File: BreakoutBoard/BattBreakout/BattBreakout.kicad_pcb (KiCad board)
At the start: 2 copper layers, 67.3 x 52.1 mm, 22 parts, among them Q4 IPB180N10S4-02, Q9 IPB180N10S4-02, U2 LM5050MK-1_NOPB, U3 LM5050MK-1_NOPB

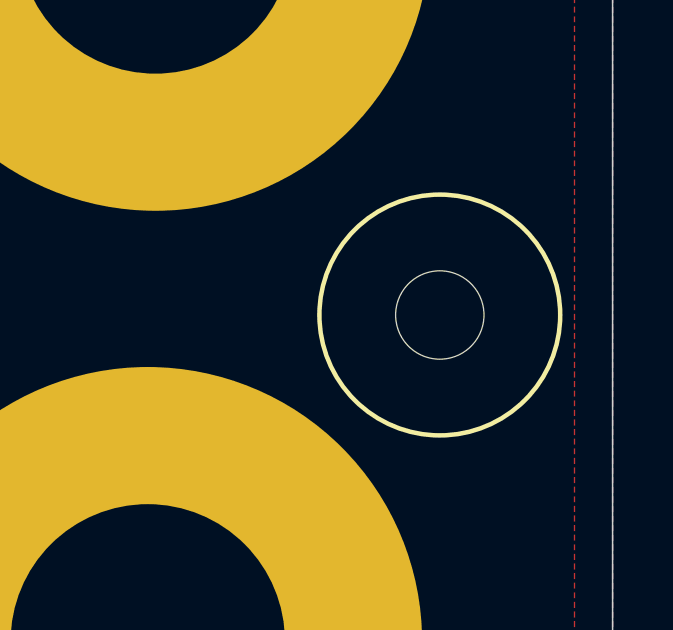
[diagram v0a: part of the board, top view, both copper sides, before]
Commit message: Added Ore to Breakout Board
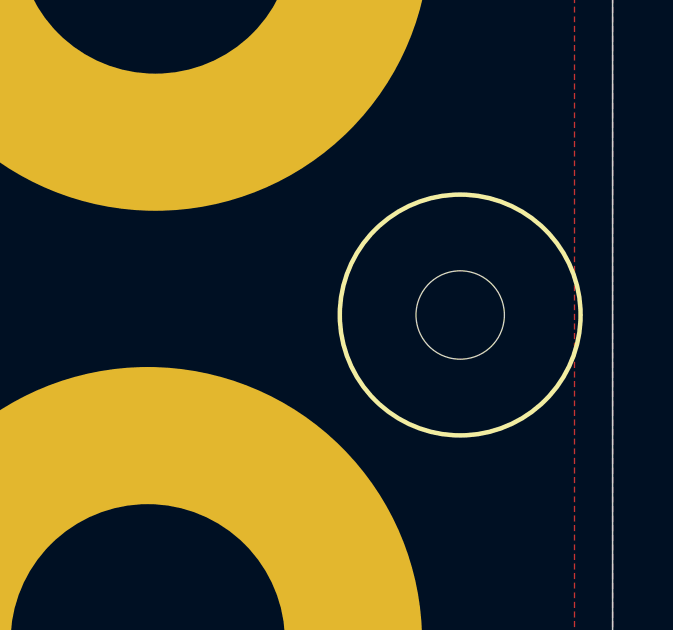
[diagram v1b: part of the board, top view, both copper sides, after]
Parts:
- added G***: LOGO, LOGO, B.Cu at (64.8, 64.1)
- moved H2 0.68 mm to (88.7, 68.7)
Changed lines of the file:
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@@
 	(footprint "MRDT_Drill_Holes:4_40_Hole_Corner"
 		(layer "F.Cu")
-		(at 88.0223 68.6957)
+		(at 88.70188 68.6957)
 		(property "Reference" "H2"
 			(at 4.00812 -3.50812 0)
@@
 		)
 	)
+	(footprint "LOGO"
+		(layer "B.Cu")
+		(at 64.77 64.135 180)
+		(property "Reference" "G***"
+			(at 0 0 0)
+			(layer "B.SilkS")
+			(effects
+				(font
+					(size 1.5 1.5)
+					(thickness 0.3)
+				)
+				(justify mirror)
+			)
+		)
+		(property "Value" "LOGO"
+			(at 0.75 0 0)
+			(layer "B.SilkS")
+			(hide yes)
+			(effects
+				(font
+					(size 1.5 1.5)
+					(thickness 0.3)
+				)
+				(justify mirror)
+			)
+		)
+		(property "Datasheet" ""
+			(at 0 0 0)
+			(layer "B.Fab")
+			(hide yes)
+			(effects
+				(font
+					(size 1.27 1.27)
+					(thickness 0.15)
+				)
+				(justify mirror)
+			)
+		)
+		(property "Description" ""
+			(at 0 0 0)
+			(layer "B.Fab")
+			(hide yes)
+			(effects
+				(font
+					(size 1.27 1.27)
+					(thickness 0.15)
+				)
+				(justify mirror)
+			)
+		)
+		(attr board_only exclude_from_pos_files exclude_from_bom)
+		(fp_poly
+			(pts
+				(xy 26.051282 0) (xy 26.051282 -26.051282) (xy 0 -26.051282) (xy -26.051282 -26.051282) (xy -26.051282 -17.910256)
+				(xy -16.282052 -17.910256) (xy -16.282052 -19.538461) (xy -13.025641 -19.538461) (xy -9.769231 -19.538461)
+				(xy -9.769231 -17.910256) (xy -9.769231 -16.282051) (xy -13.025641 -16.282051) (xy -16.282052 -16.282051)
+				(xy -16.282052 -17.910256) (xy -26.051282 -17.910256) (xy -26.051282 -13.025641) (xy 0 -13.025641)
+				(xy 0 -14.653846) (xy 0 -16.282051) (xy 1.628205 -16.282051) (xy 3.25641 -16.282051) (xy 3.25641 -17.910256)
+				(xy 3.25641 -19.538461) (xy 6.51282 -19.538461) (xy 9.76923 -19.538461) (xy 9.76923 -17.910256)
+				(xy 9.76923 -16.282051) (xy 14.653846 -16.282051) (xy 19.538461 -16.282051) (xy 19.538461 -14.653846)
+				(xy 19.538461 -13.025641) (xy 17.910256 -13.025641) (xy 16.282051 -13.025641) (xy 16.282051 -11.397435)
+				(xy 16.282051 -9.76923) (xy 13.025641 -9.76923) (xy 9.76923 -9.76923) (xy 9.76923 -11.397435) (xy 9.76923 -13.025641)
+				(xy 4.884615 -13.025641) (xy 0 -13.025641) (xy -26.051282 -13.025641) (xy -26.051282 -8.141025)
+				(xy -13.025641 -8.141025) (xy -13.025641 -9.76923) (xy -11.397436 -9.76923) (xy -9.769231 -9.76923)
+				(xy -9.769231 -8.141025) (xy -9.769231 -6.51282) (xy -11.397436 -6.51282) (xy -13.025641 -6.51282)
+				(xy -13.025641 -8.141025) (xy -26.051282 -8.141025) (xy -26.051282 -1.628205) (xy -22.794872 -1.628205)
+				(xy -22.794872 -3.25641) (xy -19.538462 -3.25641) (xy -16.282052 -3.25641) (xy -3.256411 -3.25641)
+				(xy -3.256411 -4.884615) (xy -3.256411 -6.51282) (xy 3.25641 -6.51282) (xy 9.76923 -6.51282) (xy 9.76923 -4.884615)
+				(xy 9.76923 -3.25641) (xy 8.141025 -3.25641) (xy 6.51282 -3.25641) (xy 6.51282 -1.628205) (xy 6.51282 0)
+				(xy 3.25641 0) (xy 0 0) (xy 0 -1.628205) (xy 0 -3.25641) (xy -1.628206 -3.25641) (xy -3.256411 -3.25641)
+				(xy -16.282052 -3.25641) (xy -16.282052 -1.628205) (xy -16.282052 0) (xy -19.538462 0) (xy -22.794872 0)
+				(xy -22.794872 -1.628205) (xy -26.051282 -1.628205) (xy -26.051282 0) (xy -26.051282 6.512821) (xy -16.282052 6.512821)
+				(xy -16.282052 4.884616) (xy -16.282052 3.256411) (xy -8.141026 3.256411) (xy 0 3.256411) (xy 0 4.884616)
+				(xy 0 6.512821) (xy 6.51282 6.512821) (xy 6.51282 3.256411) (xy 9.76923 3.256411) (xy 13.025641 3.256411)
+				(xy 13.025641 6.512821) (xy 13.025641 9.769231) (xy 9.76923 9.769231) (xy 6.51282 9.769231) (xy 6.51282 6.512821)
+				(xy 0 6.512821) (xy -1.628206 6.512821) (xy -3.256411 6.512821) (xy -3.256411 8.141026) (xy -3.256411 9.769231)
+				(xy -6.512821 9.769231) (xy -9.769231 9.769231) (xy -9.769231 8.141026) (xy -9.769231 6.512821)
+				(xy -13.025641 6.512821) (xy -16.282052 6.512821) (xy -26.051282 6.512821) (xy -26.051282 14.653847)
+				(xy -3.256411 14.653847) (xy -3.256411 13.025641) (xy 0 13.025641) (xy 3.25641 13.025641) (xy 3.25641 14.653847)
+				(xy 3.25641 16.282052) (xy 0 16.282052) (xy -3.256411 16.282052) (xy -3.256411 14.653847) (xy -26.051282 14.653847)
+				(xy -26.051282 17.910257) (xy -13.025641 17.910257) (xy -13.025641 16.282052) (xy -11.397436 16.282052)
+				(xy -9.769231 16.282052) (xy -9.769231 17.910257) (xy 13.025641 17.910257) (xy 13.025641 16.282052)
+				(xy 16.282051 16.282052) (xy 19.538461 16.282052) (xy 19.538461 17.910257) (xy 19.538461 19.538462)
+				(xy 16.282051 19.538462) (xy 13.025641 19.538462) (xy 13.025641 17.910257) (xy -9.769231 17.910257)
+				(xy -9.769231 19.538462) (xy -11.397436 19.538462) (xy -13.025641 19.538462) (xy -13.025641 17.910257)
+				(xy -26.051282 17.910257) (xy -26.051282 26.051282) (xy 0 26.051282) (xy 26.051282 26.051282)
+			)
+			(stroke
+				(width 0)
+				(type solid)
+			)
+			(fill yes)
+			(layer "B.SilkS")
+		)
+		(embedded_fonts no)
+	)
 	(gr_line

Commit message: Testing points started
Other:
- board text added: "Batt1+"
- board text added: "Batt2+"
- board text added: "Breakout Board, Rev 1 Mars Rover Design Team Missouri S&T, 2026 Aiden Brooks, Cohen Dummerth, Emilio Baeza, Max Thering"
- board text added: "GND"
- board text added: "OUT+"
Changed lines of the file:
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@@
 		(layer "Edge.Cuts")
+	)
+	(gr_text "Breakout Board, Rev 1\nMars Rover Design Team\nMissouri S&T, 2026\nAiden Brooks, Cohen Dummerth,\nEmilio Baeza, Max Thering"
+		(at 40.64 66.675 0)
+		(layer "F.SilkS")
+		(effects
+			(font
+				(size 0.635 0.635)
+				(thickness 0.15875)
+				(bold yes)
+			)
+			(justify left bottom)
+		)
+	)
+	(gr_text "GND\n"
+		(at 95.25 79.375 90)
+		(layer "F.SilkS")
+		(effects
+			(font
+				(size 2.54 2.54)
+				(thickness 0.635)
+				(bold yes)
+			)
+			(justify left bottom)
+		)
+	)
+	(gr_text "Batt2+"
+		(at 55.88 88.9 90)
+		(layer "F.SilkS")
+		(effects
+			(font
+				(size 2.54 2.54)
+				(thickness 0.635)
+				(bold yes)
+			)
+			(justify left bottom)
+		)
+	)
+	(gr_text "Batt1+"
+		(at 56.515 53.34 90)
+		(layer "F.SilkS")
+		(effects
+			(font
+				(size 2.54 2.54)
+				(thickness 0.635)
+				(bold yes)
+			)
+			(justify left bottom)
+		)
+	)
+	(gr_text "OUT+"
+		(at 95.885 57.785 90)
+		(layer "F.SilkS")
+		(effects
+			(font
+				(size 2.54 2.54)
+				(thickness 0.635)
+				(bold yes)
+			)
+			(justify left bottom)
+		)
 	)
 	(via

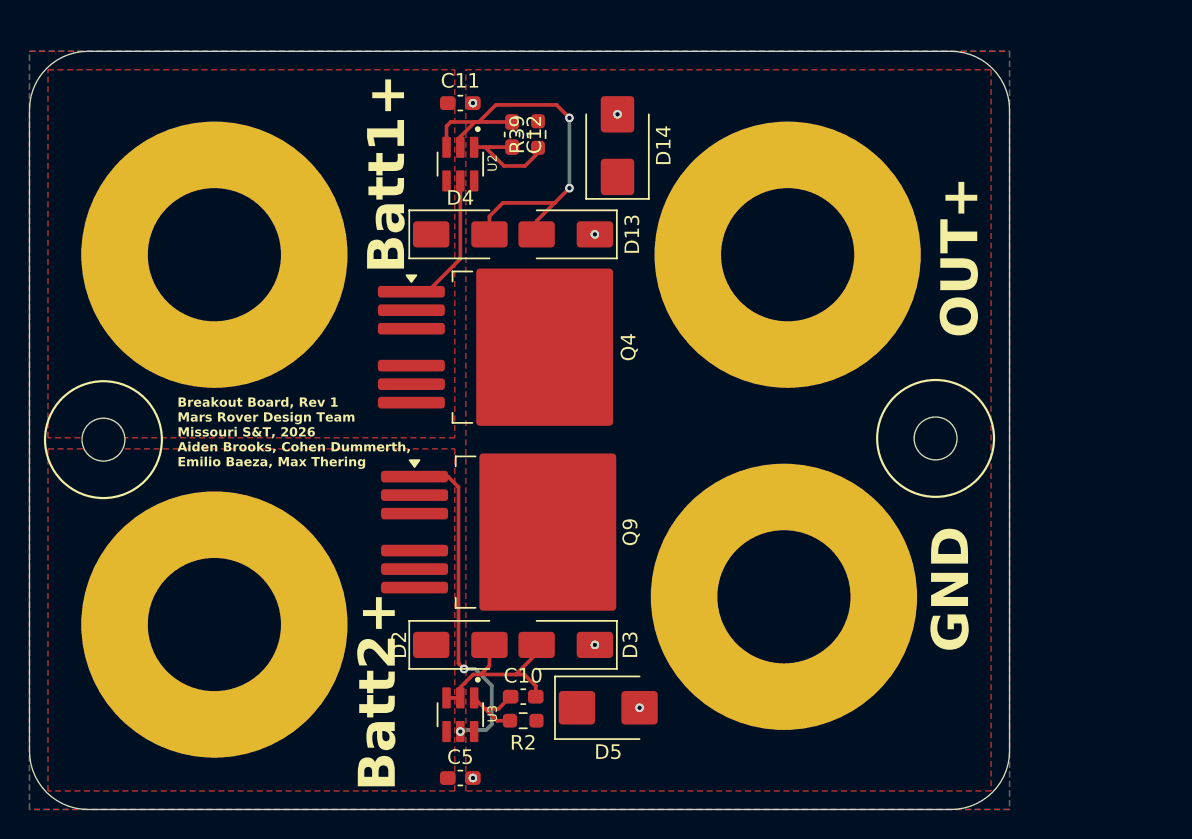
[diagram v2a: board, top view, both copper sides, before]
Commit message: Added test points and labels for op amps
-Also added a MRDT logo to the breakout board
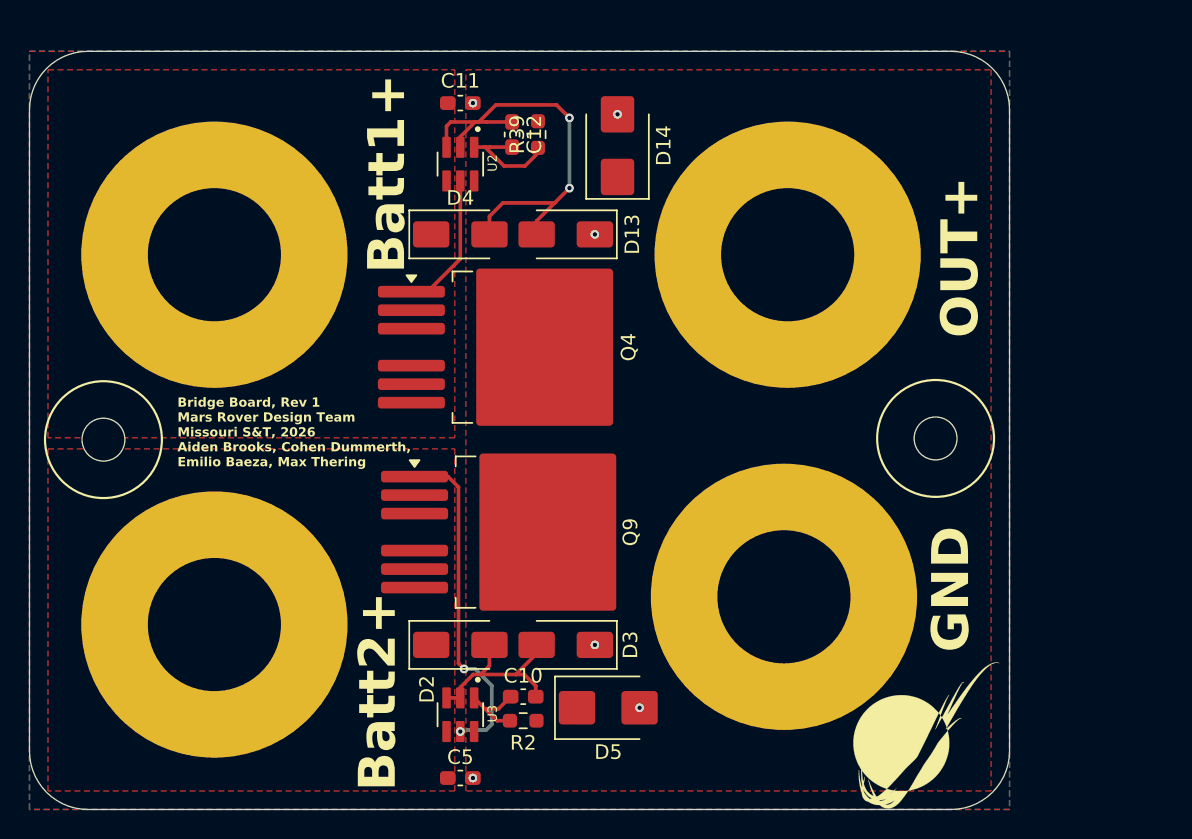
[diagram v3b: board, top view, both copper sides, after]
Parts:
- added G1: LOGO, MRDT_Silkscreens:0_MRDT_Logo_10mm, F.Cu at (92.1, 85.1)
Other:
- board text added: "Bridge Board, Rev 1 Mars Rover Design Team Missouri S&T, 2026 Aiden Brooks, Cohen Dummerth, Emilio Baeza, Max Thering"
- board text removed: "Breakout Board, Rev 1 Mars Rover Design Team Missouri S&T, 2026 Aiden Brooks, Cohen Dummerth, Emilio Baeza, Max Thering"

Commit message: Add redstone silkscreen
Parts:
- moved G*** 1.78 mm to (63.0, 64.1), turned to 0 degrees
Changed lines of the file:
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@@
 			(outputformat 1)
 			(mirror no)
-			(drillshape 1)
+			(drillshape 0)
 			(scaleselection 1)
-			(outputdirectory "")
+			(outputdirectory "BattBreakout/")
 		)
 	)
@@
 	(footprint "LOGO"
 		(layer "B.Cu")
-		(at 64.77 64.135 180)
+		(at 62.992 64.135)
 		(property "Reference" "G***"
-			(at 0 0 0)
+			(at 0 0 180)
 			(layer "B.SilkS")
+			(hide yes)
 			(effects
 				(font
@@
 		)
 		(property "Value" "LOGO"
-			(at 0.75 0 0)
+			(at 0.75 0 180)
 			(layer "B.SilkS")
 			(hide yes)
@@
 		)
 		(property "Datasheet" ""
-			(at 0 0 0)
+			(at 0 0 180)
 			(layer "B.Fab")
 			(hide yes)
@@
 		)
 		(property "Description" ""
-			(at 0 0 0)
+			(at 0 0 180)
 			(layer "B.Fab")
 			(hide yes)
@@
 		(fp_poly
 			(pts
-				(xy 26.051282 0) (xy 26.051282 -26.051282) (xy 0 -26.051282) (xy -26.051282 -26.051282) (xy -26.051282 -17.910256)
-				(xy -16.282052 -17.910256) (xy -16.282052 -19.538461) (xy -13.025641 -19.538461) (xy -9.769231 -19.538461)
-				(xy -9.769231 -17.910256) (xy -9.769231 -16.282051) (xy -13.025641 -16.282051) (xy -16.282052 -16.282051)
-				(xy -16.282052 -17.910256) (xy -26.051282 -17.910256) (xy -26.051282 -13.025641) (xy 0 -13.025641)
-				(xy 0 -14.653846) (xy 0 -16.282051) (xy 1.628205 -16.282051) (xy 3.25641 -16.282051) (xy 3.25641 -17.910256)
-				(xy 3.25641 -19.538461) (xy 6.51282 -19.538461) (xy 9.76923 -19.538461) (xy 9.76923 -17.910256)
-				(xy 9.76923 -16.282051) (xy 14.653846 -16.282051) (xy 19.538461 -16.282051) (xy 19.538461 -14.653846)
-				(xy 19.538461 -13.025641) (xy 17.910256 -13.025641) (xy 16.282051 -13.025641) (xy 16.282051 -11.397435)
-				(xy 16.282051 -9.76923) (xy 13.025641 -9.76923) (xy 9.76923 -9.76923) (xy 9.76923 -11.397435) (xy 9.76923 -13.025641)
-				(xy 4.884615 -13.025641) (xy 0 -13.025641) (xy -26.051282 -13.025641) (xy -26.051282 -8.141025)
-				(xy -13.025641 -8.141025) (xy -13.025641 -9.76923) (xy -11.397436 -9.76923) (xy -9.769231 -9.76923)
-				(xy -9.769231 -8.141025) (xy -9.769231 -6.51282) (xy -11.397436 -6.51282) (xy -13.025641 -6.51282)
-				(xy -13.025641 -8.141025) (xy -26.051282 -8.141025) (xy -26.051282 -1.628205) (xy -22.794872 -1.628205)
-				(xy -22.794872 -3.25641) (xy -19.538462 -3.25641) (xy -16.282052 -3.25641) (xy -3.256411 -3.25641)
-				(xy -3.256411 -4.884615) (xy -3.256411 -6.51282) (xy 3.25641 -6.51282) (xy 9.76923 -6.51282) (xy 9.76923 -4.884615)
-				(xy 9.76923 -3.25641) (xy 8.141025 -3.25641) (xy 6.51282 -3.25641) (xy 6.51282 -1.628205) (xy 6.51282 0)
-				(xy 3.25641 0) (xy 0 0) (xy 0 -1.628205) (xy 0 -3.25641) (xy -1.628206 -3.25641) (xy -3.256411 -3.25641)
-				(xy -16.282052 -3.25641) (xy -16.282052 -1.628205) (xy -16.282052 0) (xy -19.538462 0) (xy -22.794872 0)
-				(xy -22.794872 -1.628205) (xy -26.051282 -1.628205) (xy -26.051282 0) (xy -26.051282 6.512821) (xy -16.282052 6.512821)
-				(xy -16.282052 4.884616) (xy -16.282052 3.256411) (xy -8.141026 3.256411) (xy 0 3.256411) (xy 0 4.884616)
-				(xy 0 6.512821) (xy 6.51282 6.512821) (xy 6.51282 3.256411) (xy 9.76923 3.256411) (xy 13.025641 3.256411)
-				(xy 13.025641 6.512821) (xy 13.025641 9.769231) (xy 9.76923 9.769231) (xy 6.51282 9.769231) (xy 6.51282 6.512821)
-				(xy 0 6.512821) (xy -1.628206 6.512821) (xy -3.256411 6.512821) (xy -3.256411 8.141026) (xy -3.256411 9.769231)
-				(xy -6.512821 9.769231) (xy -9.769231 9.769231) (xy -9.769231 8.141026) (xy -9.769231 6.512821)
-				(xy -13.025641 6.512821) (xy -16.282052 6.512821) (xy -26.051282 6.512821) (xy -26.051282 14.653847)
-				(xy -3.256411 14.653847) (xy -3.256411 13.025641) (xy 0 13.025641) (xy 3.25641 13.025641) (xy 3.25641 14.653847)
-				(xy 3.25641 16.282052) (xy 0 16.282052) (xy -3.256411 16.282052) (xy -3.256411 14.653847) (xy -26.051282 14.653847)
-				(xy -26.051282 17.910257) (xy -13.025641 17.910257) (xy -13.025641 16.282052) (xy -11.397436 16.282052)
-				(xy -9.769231 16.282052) (xy -9.769231 17.910257) (xy 13.025641 17.910257) (xy 13.025641 16.282052)
-				(xy 16.282051 16.282052) (xy 19.538461 16.282052) (xy 19.538461 17.910257) (xy 19.538461 19.538462)
-				(xy 16.282051 19.538462) (xy 13.025641 19.538462) (xy 13.025641 17.910257) (xy -9.769231 17.910257)
-				(xy -9.769231 19.538462) (xy -11.397436 19.538462) (xy -13.025641 19.538462) (xy -13.025641 17.910257)
-				(xy -26.051282 17.910257) (xy -26.051282 26.051282) (xy 0 26.051282) (xy 26.051282 26.051282)
+				(xy 9.912195 0) (xy 9.912195 -9.912195) (xy 0 -9.912195) (xy -9.912195 -9.912195) (xy -9.912195 -6.814634)
+				(xy -6.195122 -6.814634) (xy -6.195122 -7.434146) (xy -4.956098 -7.434146) (xy -3.717074 -7.434146)
+				(xy -3.717074 -6.814634) (xy -3.717074 -6.195122) (xy -4.956098 -6.195122) (xy -6.195122 -6.195122)
+				(xy -6.195122 -6.814634) (xy -9.912195 -6.814634) (xy -9.912195 -4.956097) (xy 0 -4.956097) (xy 0 -5.575609)
+				(xy 0 -6.195122) (xy 0.619512 -6.195122) (xy 1.239024 -6.195122) (xy 1.239024 -6.814634) (xy 1.239024 -7.434146)
+				(xy 2.478048 -7.434146) (xy 3.717073 -7.434146) (xy 3.717073 -6.814634) (xy 3.717073 -6.195122)
+				(xy 5.575609 -6.195122) (xy 7.434146 -6.195122) (xy 7.434146 -5.575609) (xy 7.434146 -4.956097)
+				(xy 6.814634 -4.956097) (xy 6.195122 -4.956097) (xy 6.195122 -4.336585) (xy 6.195122 -3.717073)
+				(xy 4.956097 -3.717073) (xy 3.717073 -3.717073) (xy 3.717073 -4.336585) (xy 3.717073 -4.956097)
+				(xy 1.858536 -4.956097) (xy 0 -4.956097) (xy -9.912195 -4.956097) (xy -9.912195 -3.097561) (xy -4.956098 -3.097561)
+				(xy -4.956098 -3.717073) (xy -4.336586 -3.717073) (xy -3.717074 -3.717073) (xy -3.717074 -3.097561)
+				(xy -3.717074 -2.478048) (xy -4.336586 -2.478048) (xy -4.956098 -2.478048) (xy -4.956098 -3.097561)
+				(xy -9.912195 -3.097561) (xy -9.912195 -0.619512) (xy -8.673171 -0.619512) (xy -8.673171 -1.239024)
+				(xy -7.434147 -1.239024) (xy -6.195122 -1.239024) (xy -1.239025 -1.239024) (xy -1.239025 -1.858536)
+				(xy -1.239025 -2.478048) (xy 1.239024 -2.478048) (xy 3.717073 -2.478048) (xy 3.717073 -1.858536)
+				(xy 3.717073 -1.239024) (xy 3.097561 -1.239024) (xy 2.478048 -1.239024) (xy 2.478048 -0.619512)
+				(xy 2.478048 0) (xy 1.239024 0) (xy 0 0) (xy 0 -0.619512) (xy 0 -1.239024) (xy -0.619513 -1.239024)
+				(xy -1.239025 -1.239024) (xy -6.195122 -1.239024) (xy -6.195122 -0.619512) (xy -6.195122 0) (xy -7.434147 0)
+				(xy -8.673171 0) (xy -8.673171 -0.619512) (xy -9.912195 -0.619512) (xy -9.912195 0) (xy -9.912195 2.478049)
+				(xy -6.195122 2.478049) (xy -6.195122 1.858537) (xy -6.195122 1.239025) (xy -3.097561 1.239025)
+				(xy 0 1.239025) (xy 0 1.858537) (xy 0 2.478049) (xy 2.478048 2.478049) (xy 2.478048 1.239025) (xy 3.717073 1.239025)
+				(xy 4.956097 1.239025) (xy 4.956097 2.478049) (xy 4.956097 3.717074) (xy 3.717073 3.717074) (xy 2.478048 3.717074)
+				(xy 2.478048 2.478049) (xy 0 2.478049) (xy -0.619513 2.478049) (xy -1.239025 2.478049) (xy -1.239025 3.097561)
+				(xy -1.239025 3.717074) (xy -2.478049 3.717074) (xy -3.717074 3.717074) (xy -3.717074 3.097561)
+				(xy -3.717074 2.478049) (xy -4.956098 2.478049) (xy -6.195122 2.478049) (xy -9.912195 2.478049)
+				(xy -9.912195 5.57561) (xy -1.239025 5.57561) (xy -1.239025 4.956098) (xy 0 4.956098) (xy 1.239024 4.956098)
+				(xy 1.239024 5.57561) (xy 1.239024 6.195122) (xy 0 6.195122) (xy -1.239025 6.195122) (xy -1.239025 5.57561)
+				(xy -9.912195 5.57561) (xy -9.912195 6.814635) (xy -4.956098 6.814635) (xy -4.956098 6.195122) (xy -4.336586 6.195122)
+				(xy -3.717074 6.195122) (xy -3.717074 6.814635) (xy 4.956097 6.814635) (xy 4.956097 6.195122) (xy 6.195122 6.195122)
+				(xy 7.434146 6.195122) (xy 7.434146 6.814635) (xy 7.434146 7.434147) (xy 6.195122 7.434147) (xy 4.956097 7.434147)
+				(xy 4.956097 6.814635) (xy -3.717074 6.814635) (xy -3.717074 7.434147) (xy -4.336586 7.434147) (xy -4.956098 7.434147)
+				(xy -4.956098 6.814635) (xy -9.912195 6.814635) (xy -9.912195 9.912195) (xy 0 9.912195) (xy 9.912195 9.912195)
 			)
 			(stroke
@@
 		(layer "Edge.Cuts")
 	)
+	(gr_line
+		(start 64.135 38.1)
+		(end 64.135 90.17)
+		(stroke
+			(width 0.1)
+			(type default)
+		)
+		(layer "B.Fab")
+	)
+	(gr_line
+		(start 97.79 64.135)
+		(end 30.48 64.135)
+		(stroke
+			(width 0.1)
+			(type default)
+		)
+		(layer "B.Fab")
+	)
 	(gr_text "Bridge Board, Rev 1\nMars Rover Design Team\nMissouri S&T, 2026\nAiden Brooks, Cohen Dummerth,\nEmilio Baeza, Max Thering"
